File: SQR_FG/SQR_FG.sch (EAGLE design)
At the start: 15 parts, among them IC1 MEGA328P, IC2 NJM7032, Q1 16MHz, SW1 EC12E_SW

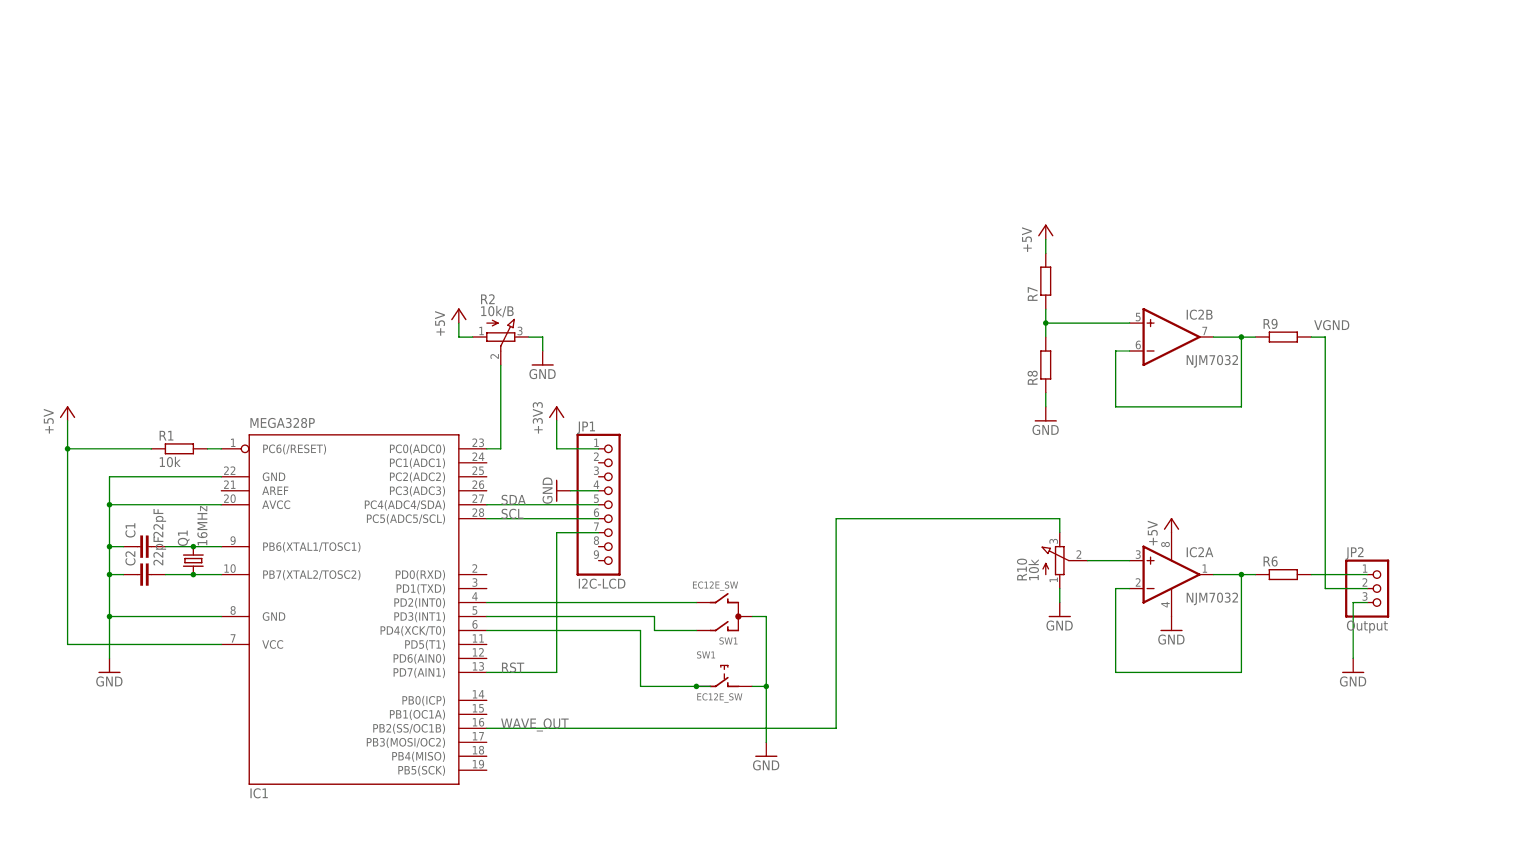
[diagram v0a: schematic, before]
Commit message: SQR_FG MOS-FET Switch
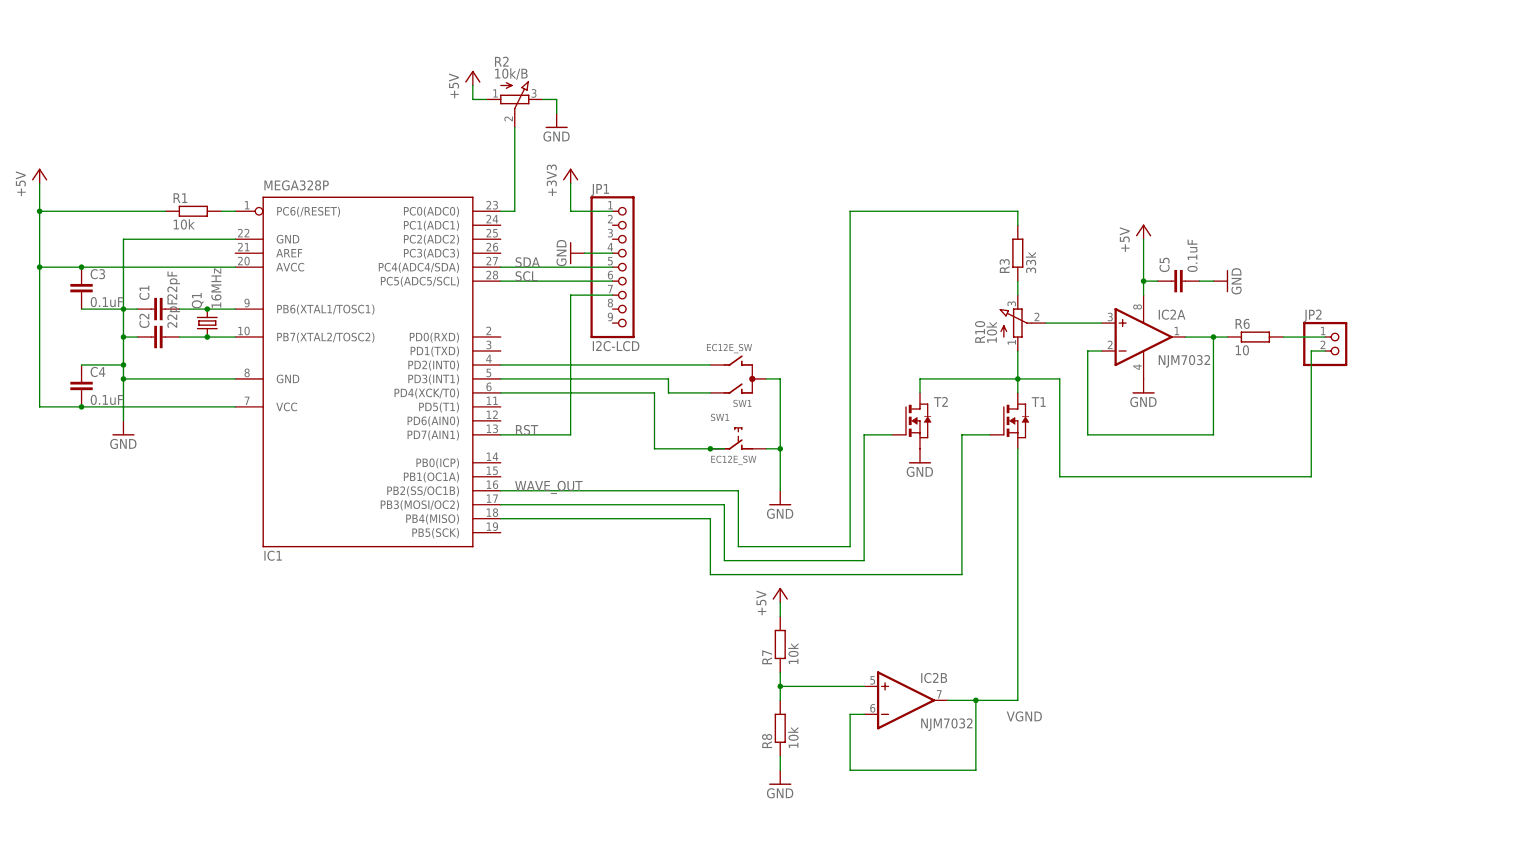
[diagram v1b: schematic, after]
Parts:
- removed R9: (no value), rcl:R-EU_0207/7
- added C3, C4, C5: 0.1uF, rcl:C-EU025-024X044
- added R3: 33k, rcl:R-EU_0207/7
- added T1, T2: (no value), zetex:NMOSE3L
- JP2: value Output -> (none); device pinhead:PINHD-1X3 -> pinhead:PINHD-1X2
- R6: value (none) -> 10
- R7, R8: value (none) -> 10k
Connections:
- removed net N$14: IC2B.-IN, IC2B.OUT, R9.1
- new net N$12: IC1.PB3(MOSI/OC2), T2.G
- new net N$13: IC1.PB4(MISO), T1.G
- new net N$6: JP2.2, R10.A, T1.D, T2.D
- new net N$8: R10.E, R3.1
- net +5V: now also C3.1, C4.2, C5.1, IC1.AVCC
- net GND: now also C3.2, C4.1, C5.2, T2.S; no longer IC1.AVCC, JP2.3, R10.A
- net VGND: now also IC2B.-IN, IC2B.OUT, T1.S; no longer JP2.2, R9.2
- net WAVE_OUT: now also R3.2; no longer R10.E
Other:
- moved on the sheet: C1, C2, IC1, IC2A, IC2B, JP1, Q1, R1, R10, R2, R6, R7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

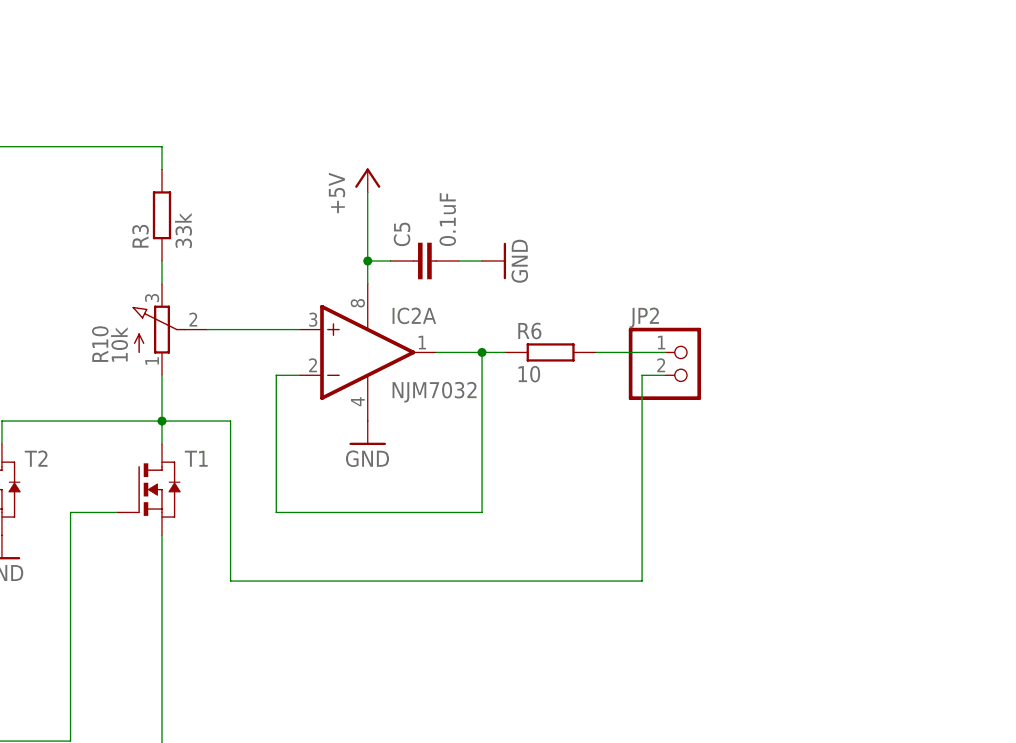
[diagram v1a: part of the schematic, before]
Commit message: SQR_FG Add 2nd VCVS LPF
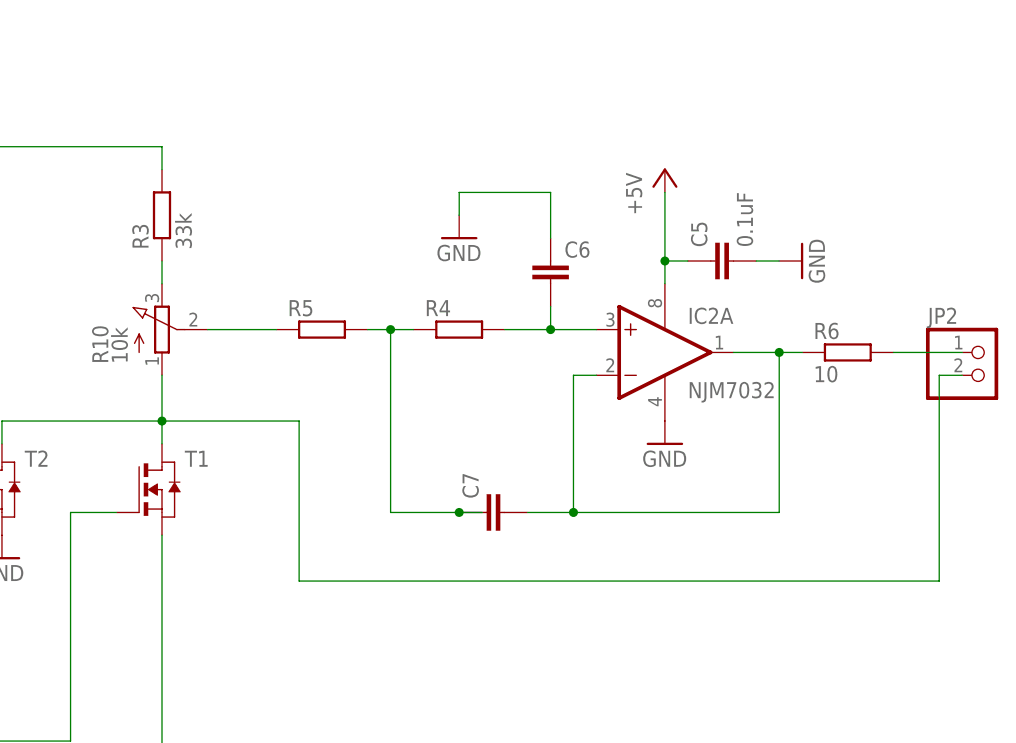
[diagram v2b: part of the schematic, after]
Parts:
- added C6, C7: (no value), rcl:C-EU025-024X044
- added R4, R5: (no value), rcl:R-EU_0207/7
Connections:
- new net N$14: C6.2, IC2A.+IN, R4.2
- new net N$15: R5.1
- net GND: now also C6.1
- net N$16: now also C7.2
- net N$4: now also C7.1, R4.1, R5.2; no longer IC2A.+IN, R10.S
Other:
- moved on the sheet: C5, IC2A, JP2, R6
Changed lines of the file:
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@@
 <part name="JP2" library="pinhead" deviceset="PINHD-1X2" device=""/>
 <part name="R3" library="rcl" deviceset="R-EU_" device="0207/7" value="33k"/>
+<part name="R4" library="rcl" deviceset="R-EU_" device="0207/7"/>
+<part name="R5" library="rcl" deviceset="R-EU_" device="0207/7"/>
+<part name="C6" library="rcl" deviceset="C-EU" device="025-024X044"/>
+<part name="C7" library="rcl" deviceset="C-EU" device="025-024X044"/>
+<part name="GND6" library="supply1" deviceset="GND" device=""/>
 </parts>
 <sheets>
@@
 <instance part="SW1" gate="G$2" x="132.08" y="73.66"/>
 <instance part="GND4" gate="1" x="139.7" y="63.5"/>
-<instance part="P+3" gate="1" x="205.74" y="114.3"/>
-<instance part="GND7" gate="1" x="205.74" y="83.82"/>
-<instance part="IC2" gate="A" x="205.74" y="93.98"/>
+<instance part="P+3" gate="1" x="238.76" y="114.3"/>
+<instance part="GND7" gate="1" x="238.76" y="83.82"/>
+<instance part="IC2" gate="A" x="238.76" y="93.98"/>
 <instance part="IC2" gate="B" x="162.56" y="27.94"/>
-<instance part="IC2" gate="P" x="205.74" y="93.98"/>
-<instance part="R6" gate="G$1" x="226.06" y="93.98"/>
+<instance part="IC2" gate="P" x="238.76" y="93.98"/>
+<instance part="R6" gate="G$1" x="259.08" y="93.98"/>
 <instance part="R7" gate="G$1" x="139.7" y="38.1" rot="R90"/>
 <instance part="R8" gate="G$1" x="139.7" y="22.86" rot="R90"/>
@@
 <instance part="T2" gate="A" x="165.1" y="78.74"/>
 <instance part="GND10" gate="1" x="165.1" y="71.12"/>
-<instance part="C5" gate="G$1" x="210.82" y="104.14" rot="R90"/>
-<instance part="GND5" gate="1" x="220.98" y="104.14" rot="R90"/>
-<instance part="JP2" gate="G$1" x="241.3" y="91.44"/>
+<instance part="C5" gate="G$1" x="243.84" y="104.14" rot="R90"/>
+<instance part="GND5" gate="1" x="254" y="104.14" rot="R90"/>
+<instance part="JP2" gate="G$1" x="274.32" y="91.44"/>
 <instance part="R3" gate="G$1" x="182.88" y="109.22" rot="R90"/>
+<instance part="R4" gate="G$1" x="215.9" y="96.52"/>
+<instance part="R5" gate="G$1" x="200.66" y="96.52"/>
+<instance part="C6" gate="G$1" x="226.06" y="104.14"/>
+<instance part="C7" gate="G$1" x="218.44" y="76.2" rot="R90"/>
+<instance part="GND6" gate="1" x="215.9" y="106.68"/>
 </instances>
 <busses>
@@
 <pinref part="C5" gate="G$1" pin="2"/>
 <pinref part="GND5" gate="1" pin="GND"/>
-<wire x1="218.44" y1="104.14" x2="215.9" y2="104.14" width="0.1524" layer="91"/>
+<wire x1="251.46" y1="104.14" x2="248.92" y2="104.14" width="0.1524" layer="91"/>
+</segment>
+<segment>
+<pinref part="C6" gate="G$1" pin="1"/>
+<wire x1="226.06" y1="106.68" x2="226.06" y2="111.76" width="0.1524" layer="91"/>
+<wire x1="226.06" y1="111.76" x2="215.9" y2="111.76" width="0.1524" layer="91"/>
+<pinref part="GND6" gate="1" pin="GND"/>
+<wire x1="215.9" y1="111.76" x2="215.9" y2="109.22" width="0.1524" layer="91"/>
 </segment>
 </net>
@@
 <segment>
 <pinref part="IC2" gate="P" pin="V+"/>
-<wire x1="205.74" y1="101.6" x2="205.74" y2="104.14" width="0.1524" layer="91"/>
+<wire x1="238.76" y1="101.6" x2="238.76" y2="104.14" width="0.1524" layer="91"/>
 <pinref part="P+3" gate="1" pin="+5V"/>
 <pinref part="C5" gate="G$1" pin="1"/>
-<wire x1="205.74" y1="104.14" x2="205.74" y2="111.76" width="0.1524" layer="91"/>
-<wire x1="208.28" y1="104.14" x2="205.74" y2="104.14" width="0.1524" layer="91"/>
-<junction x="205.74" y="104.14"/>
+<wire x1="238.76" y1="104.14" x2="238.76" y2="111.76" width="0.1524" layer="91"/>
+<wire x1="241.3" y1="104.14" x2="238.76" y2="104.14" width="0.1524" layer="91"/>
+<junction x="238.76" y="104.14"/>
 </segment>
 </net>
@@
 <net name="N$16" class="0">
 <segment>
-<wire x1="198.12" y1="91.44" x2="195.58" y2="91.44" width="0.1524" layer="91"/>
-<wire x1="195.58" y1="91.44" x2="195.58" y2="76.2" width="0.1524" layer="91"/>
-<wire x1="195.58" y1="76.2" x2="218.44" y2="76.2" width="0.1524" layer="91"/>
-<wire x1="218.44" y1="76.2" x2="218.44" y2="93.98" width="0.1524" layer="91"/>
-<wire x1="218.44" y1="93.98" x2="213.36" y2="93.98" width="0.1524" layer="91"/>
+<wire x1="231.14" y1="91.44" x2="228.6" y2="91.44" width="0.1524" layer="91"/>
+<wire x1="228.6" y1="91.44" x2="228.6" y2="76.2" width="0.1524" layer="91"/>
+<wire x1="228.6" y1="76.2" x2="251.46" y2="76.2" width="0.1524" layer="91"/>
+<wire x1="251.46" y1="76.2" x2="251.46" y2="93.98" width="0.1524" layer="91"/>
+<wire x1="251.46" y1="93.98" x2="246.38" y2="93.98" width="0.1524" layer="91"/>
 <pinref part="IC2" gate="A" pin="-IN"/>
 <pinref part="IC2" gate="A" pin="OUT"/>
 <pinref part="R6" gate="G$1" pin="1"/>
-<wire x1="220.98" y1="93.98" x2="218.44" y2="93.98" width="0.1524" layer="91"/>
-<junction x="218.44" y="93.98"/>
+<wire x1="254" y1="93.98" x2="251.46" y2="93.98" width="0.1524" layer="91"/>
+<junction x="251.46" y="93.98"/>
+<pinref part="C7" gate="G$1" pin="2"/>
+<wire x1="223.52" y1="76.2" x2="228.6" y2="76.2" width="0.1524" layer="91"/>
+<junction x="228.6" y="76.2"/>
 </segment>
 </net>
@@
 <segment>
 <pinref part="R6" gate="G$1" pin="2"/>
-<wire x1="231.14" y1="93.98" x2="238.76" y2="93.98" width="0.1524" layer="91"/>
+<wire x1="264.16" y1="93.98" x2="271.78" y2="93.98" width="0.1524" layer="91"/>
 <pinref part="JP2" gate="G$1" pin="1"/>
 </segment>
@@
 <wire x1="154.94" y1="30.48" x2="139.7" y2="30.48" width="0.1524" layer="91"/>
 <junction x="139.7" y="30.48"/>
-</segment>
-</net>
-<net name="N$4" class="0">
-<segment>
-<pinref part="R10" gate="G$1" pin="S"/>
-<pinref part="IC2" gate="A" pin="+IN"/>
-<wire x1="187.96" y1="96.52" x2="198.12" y2="96.52" width="0.1524" layer="91"/>
 </segment>
 </net>
@@
 <wire x1="165.1" y1="86.36" x2="182.88" y2="86.36" width="0.1524" layer="91"/>
 <junction x="182.88" y="86.36"/>
-<wire x1="182.88" y1="86.36" x2="190.5" y2="86.36" width="0.1524" layer="91"/>
-<wire x1="190.5" y1="86.36" x2="190.5" y2="68.58" width="0.1524" layer="91"/>
-<wire x1="190.5" y1="68.58" x2="236.22" y2="68.58" width="0.1524" layer="91"/>
-<wire x1="236.22" y1="68.58" x2="236.22" y2="91.44" width="0.1524" layer="91"/>
+<wire x1="182.88" y1="86.36" x2="198.12" y2="86.36" width="0.1524" layer="91"/>
+<wire x1="198.12" y1="86.36" x2="198.12" y2="68.58" width="0.1524" layer="91"/>
+<wire x1="198.12" y1="68.58" x2="269.24" y2="68.58" width="0.1524" layer="91"/>
+<wire x1="269.24" y1="68.58" x2="269.24" y2="91.44" width="0.1524" layer="91"/>
 <pinref part="JP2" gate="G$1" pin="2"/>
-<wire x1="238.76" y1="91.44" x2="236.22" y2="91.44" width="0.1524" layer="91"/>
+<wire x1="271.78" y1="91.44" x2="269.24" y2="91.44" width="0.1524" layer="91"/>
 </segment>
 </net>
@@
 </segment>
 </net>
+<net name="N$4" class="0">
+<segment>
+<pinref part="R5" gate="G$1" pin="2"/>
+<pinref part="R4" gate="G$1" pin="1"/>
+<wire x1="205.74" y1="96.52" x2="208.28" y2="96.52" width="0.1524" layer="91"/>
+<wire x1="208.28" y1="96.52" x2="210.82" y2="96.52" width="0.1524" layer="91"/>
+<wire x1="218.44" y1="76.2" x2="215.9" y2="76.2" width="0.1524" layer="91"/>
+<wire x1="215.9" y1="76.2" x2="208.28" y2="76.2" width="0.1524" layer="91"/>
+<wire x1="208.28" y1="76.2" x2="208.28" y2="96.52" width="0.1524" layer="91"/>
+<junction x="208.28" y="96.52"/>
+<pinref part="C7" gate="G$1" pin="1"/>
+<junction x="215.9" y="76.2"/>
+</segment>
+</net>
+<net name="N$14" class="0">
+<segment>
+<pinref part="R4" gate="G$1" pin="2"/>
+<pinref part="IC2" gate="A" pin="+IN"/>
+<wire x1="220.98" y1="96.52" x2="226.06" y2="96.52" width="0.1524" layer="91"/>
+<pinref part="C6" gate="G$1" pin="2"/>
+<wire x1="226.06" y1="96.52" x2="231.14" y2="96.52" width="0.1524" layer="91"/>
+<wire x1="226.06" y1="99.06" x2="226.06" y2="96.52" width="0.1524" layer="91"/>
+<junction x="226.06" y="96.52"/>
+</segment>
+</net>
+<net name="N$15" class="0">
+<segment>
+<pinref part="R5" gate="G$1" pin="1"/>
+<wire x1="195.58" y1="96.52" x2="187.96" y2="96.52" width="0.1524" layer="91"/>
+</segment>
+</net>
